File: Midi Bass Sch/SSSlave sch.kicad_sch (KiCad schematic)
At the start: 11 parts, among them J4 A SLAVE ISCP, J5 Pick Unit, U3 PIC16F1789

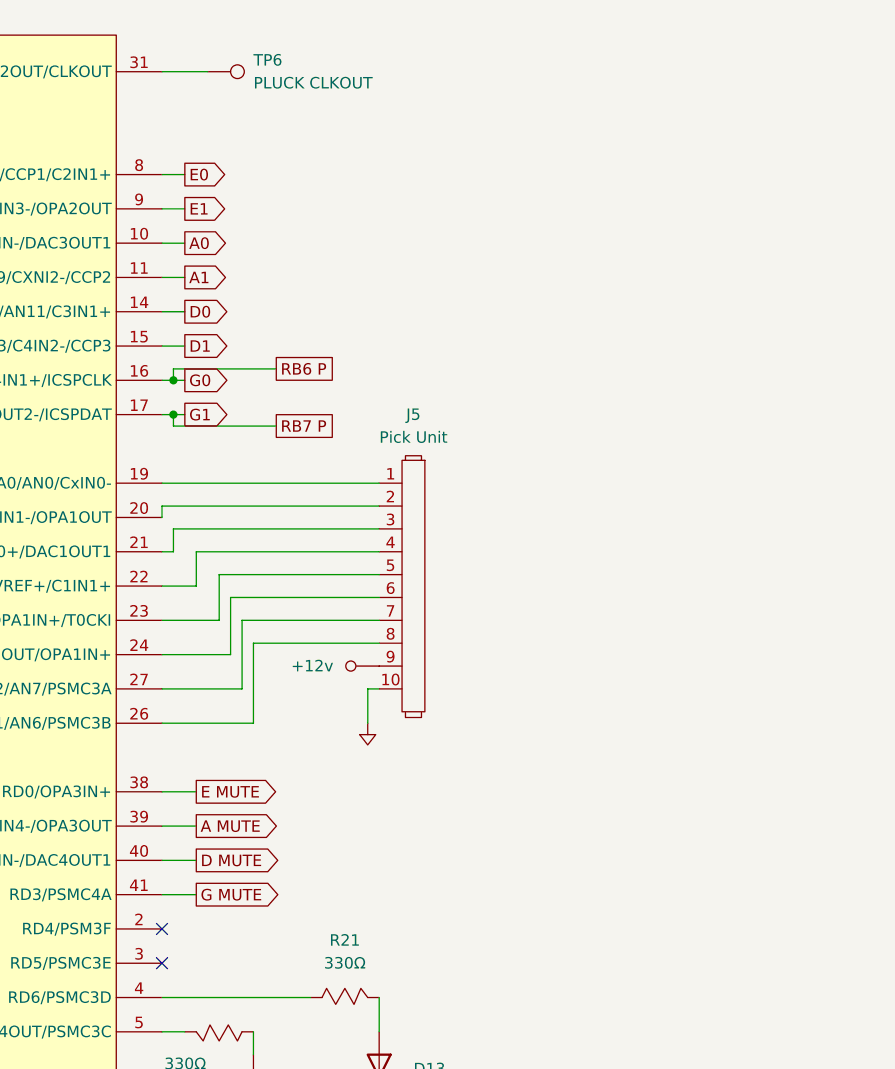
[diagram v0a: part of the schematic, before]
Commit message: working on final troubleshooting sections, modified pluck slave to header connections
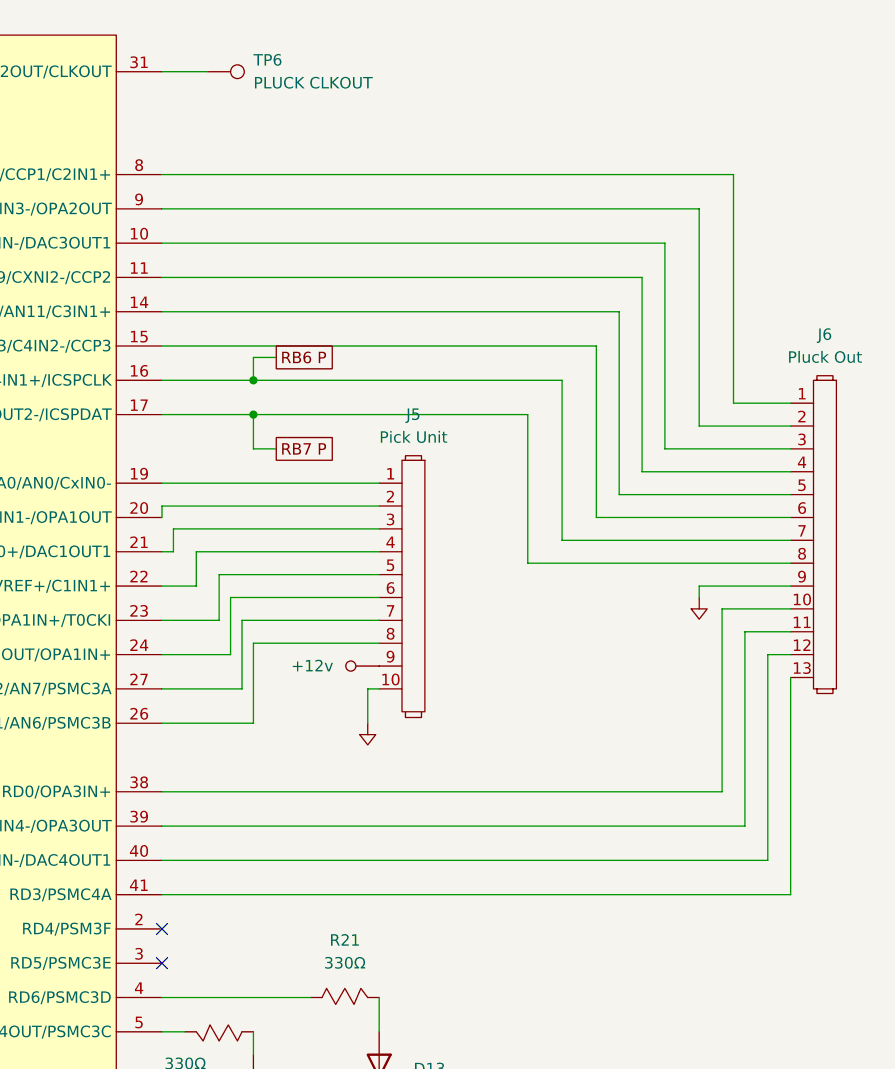
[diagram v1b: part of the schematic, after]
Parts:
- added J6: Pluck Out, symbol Owen's Symbols:Header_1x13
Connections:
- net GND: now also J6.9
- net A MUTE: no longer names the net of U3.39 (RD1/CxIN4-/OPA3OUT)
- net A MUTE: now also J6.11
- net A0: no longer names the net of U3.10 (RB2/AN8/OPA2IN-/DAC3OUT1)
- net A0: now also J6.3
- net A1: no longer names the net of U3.11 (RB3/AN9/CXNI2-/CCP2)
- net A1: now also J6.4
- net D MUTE: no longer names the net of U3.40 (RD2/OPA3IN-/DAC4OUT1)
- net D MUTE: now also J6.12
- net D0: no longer names the net of U3.14 (RB4/AN11/C3IN1+)
- net D0: now also J6.5
- net D1: no longer names the net of U3.15 (RB5/AN13/C4IN2-/CCP3)
- net D1: now also J6.6
- net E MUTE: no longer names the net of U3.38 (RD0/OPA3IN+)
- net E MUTE: now also J6.10
- net E0: no longer names the net of U3.8 (RB0/AN12/CCP1/C2IN1+)
- net E0: now also J6.1
- net E1: no longer names the net of U3.9 (RB1/AN10/CxIN3-/OPA2OUT)
- net E1: now also J6.2
- net G MUTE: no longer names the net of U3.41 (RD3/PSMC4A)
- net G MUTE: now also J6.13
- net G0 renamed RB6 P
- net RB6 P: now also J6.7
- net G1 renamed RB7 P
- net RB7 P: now also J6.8

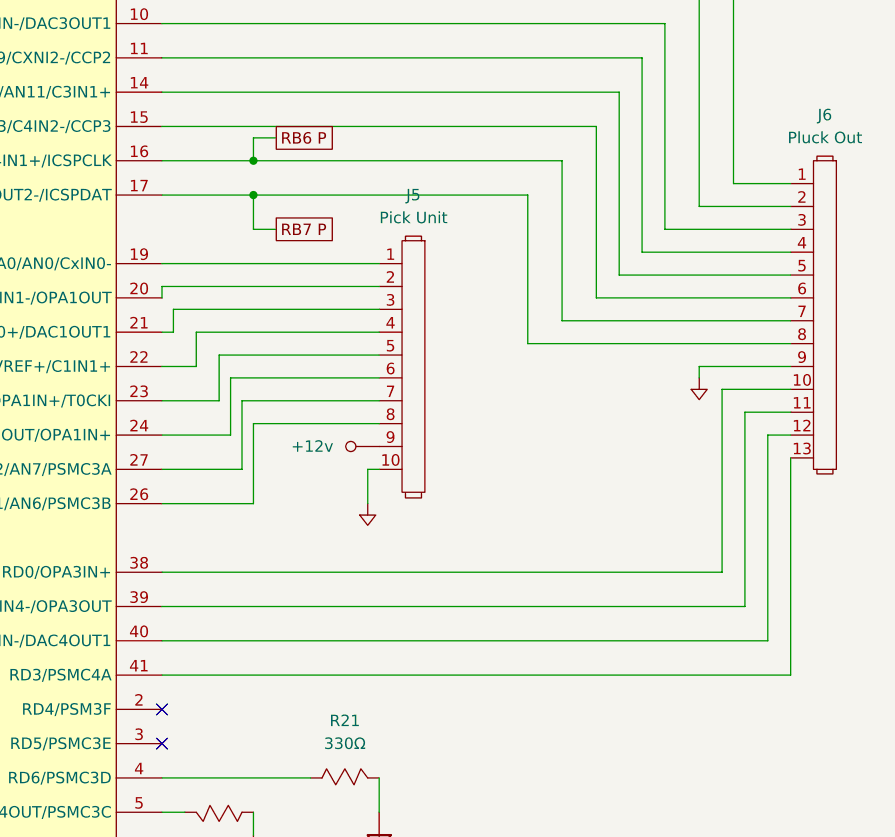
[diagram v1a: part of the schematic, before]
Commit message: updated plucking schematic to label line
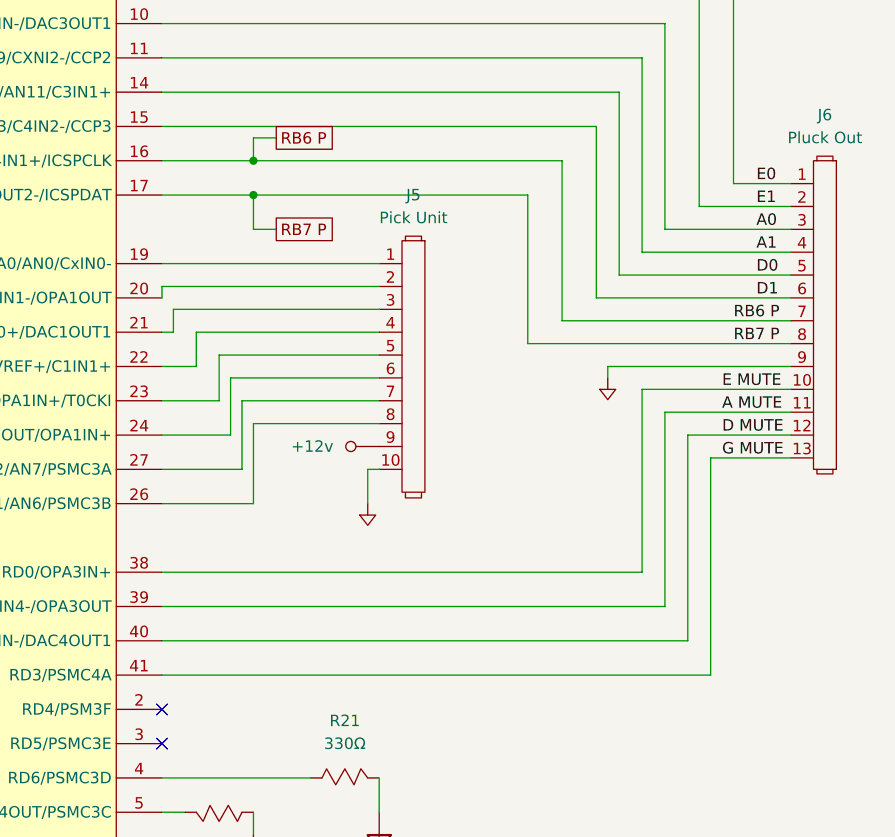
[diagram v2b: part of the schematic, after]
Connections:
- net A0: now reaches J6.3, U3.10 (RB2/AN8/OPA2IN-/DAC3OUT1)
- net A1: now reaches J6.4, U3.11 (RB3/AN9/CXNI2-/CCP2)
- net D0: now reaches J6.5, U3.14 (RB4/AN11/C3IN1+)
- net D1: now reaches J6.6, U3.15 (RB5/AN13/C4IN2-/CCP3)
- net E MUTE: now reaches J6.10, U3.38 (RD0/OPA3IN+)
- net A MUTE: now reaches J6.11, U3.39 (RD1/CxIN4-/OPA3OUT)
- net D MUTE: now reaches J6.12, U3.40 (RD2/OPA3IN-/DAC4OUT1)
- net G MUTE: now reaches J6.13, U3.41 (RD3/PSMC4A)
- net E0: now reaches J6.1, U3.8 (RB0/AN12/CCP1/C2IN1+)
- net E1: now reaches J6.2, U3.9 (RB1/AN10/CxIN3-/OPA2OUT)
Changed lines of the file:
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@@
 	(wire
 		(pts
-			(xy 228.6 92.71) (xy 233.68 92.71)
+			(xy 219.71 92.71) (xy 233.68 92.71)
 		)
 		(stroke
@@
 	(wire
 		(pts
-			(xy 233.68 121.92) (xy 233.68 97.79)
+			(xy 224.79 121.92) (xy 224.79 97.79)
 		)
 		(stroke
@@
 	(wire
 		(pts
-			(xy 228.6 114.3) (xy 228.6 92.71)
+			(xy 219.71 114.3) (xy 219.71 92.71)
 		)
 		(stroke
@@
 	(wire
 		(pts
-			(xy 163.83 118.11) (xy 231.14 118.11)
+			(xy 163.83 118.11) (xy 222.25 118.11)
 		)
 		(stroke
@@
 	(wire
 		(pts
-			(xy 226.06 110.49) (xy 226.06 90.17)
+			(xy 217.17 110.49) (xy 217.17 90.17)
 		)
 		(stroke
@@
 	(wire
 		(pts
-			(xy 163.83 121.92) (xy 233.68 121.92)
+			(xy 163.83 121.92) (xy 224.79 121.92)
 		)
 		(stroke
@@
 	(wire
 		(pts
-			(xy 233.68 87.63) (xy 223.52 87.63)
+			(xy 233.68 87.63) (xy 213.36 87.63)
 		)
 		(stroke
@@
 	(wire
 		(pts
-			(xy 231.14 118.11) (xy 231.14 95.25)
+			(xy 222.25 118.11) (xy 222.25 95.25)
 		)
 		(stroke
@@
 	(wire
 		(pts
-			(xy 231.14 95.25) (xy 233.68 95.25)
+			(xy 222.25 95.25) (xy 233.68 95.25)
 		)
 		(stroke
@@
 	(wire
 		(pts
-			(xy 163.83 110.49) (xy 226.06 110.49)
+			(xy 163.83 110.49) (xy 217.17 110.49)
 		)
 		(stroke
@@
 	(wire
 		(pts
-			(xy 226.06 90.17) (xy 233.68 90.17)
+			(xy 217.17 90.17) (xy 233.68 90.17)
 		)
 		(stroke
@@
 	(wire
 		(pts
-			(xy 163.83 114.3) (xy 228.6 114.3)
+			(xy 163.83 114.3) (xy 219.71 114.3)
 		)
 		(stroke
@@
 	(wire
 		(pts
-			(xy 223.52 87.63) (xy 223.52 88.9)
+			(xy 213.36 87.63) (xy 213.36 88.9)
 		)
 		(stroke
@@
 	(wire
 		(pts
+			(xy 224.79 97.79) (xy 233.68 97.79)
+		)
+		(stroke
+			(width 0)
+			(type default)
+		)
+	)
+	(wire
+		(pts
 			(xy 173.99 72.39) (xy 173.99 68.58)
 		)
@@
 			(width 0)
 			(type default)
+		)
+	)
+	(label "E0"
+		(at 229.87 67.31 0)
+		(fields_autoplaced yes)
+		(effects
+			(font
+				(size 1.27 1.27)
+			)
+			(justify left bottom)
+		)
+	)
+	(label "A1"
+		(at 229.87 74.93 0)
+		(fields_autoplaced yes)
+		(effects
+			(font
+				(size 1.27 1.27)
+			)
+			(justify left bottom)
+		)
+	)
+	(label "RB6 P"
+		(at 227.33 82.55 0)
+		(fields_autoplaced yes)
+		(effects
+			(font
+				(size 1.27 1.27)
+			)
+			(justify left bottom)
+		)
+	)
+	(label "E MUTE"
+		(at 226.06 90.17 0)
+		(fields_autoplaced yes)
+		(effects
+			(font
+				(size 1.27 1.27)
+			)
+			(justify left bottom)
+		)
+	)
+	(label "A0"
+		(at 229.87 72.39 0)
+		(fields_autoplaced yes)
+		(effects
+			(font
+				(size 1.27 1.27)
+			)
+			(justify left bottom)
+		)
+	)
+	(label "D0"
+		(at 229.87 77.47 0)
+		(fields_autoplaced yes)
+		(effects
+			(font
+				(size 1.27 1.27)
+			)
+			(justify left bottom)
+		)
+	)
+	(label "D MUTE"
+		(at 226.06 95.25 0)
+		(fields_autoplaced yes)
+		(effects
+			(font
+				(size 1.27 1.27)
+			)
+			(justify left bottom)
+		)
+	)
+	(label "E1"
+		(at 229.87 69.85 0)
+		(fields_autoplaced yes)
+		(effects
+			(font
+				(size 1.27 1.27)
+			)
+			(justify left bottom)
+		)
+	)
+	(label "A MUTE"
+		(at 226.06 92.71 0)
+		(fields_autoplaced yes)
+		(effects
+			(font
+				(size 1.27 1.27)
+			)
+			(justify left bottom)
+		)
+	)
+	(label "G MUTE"
+		(at 226.06 97.79 0)
+		(fields_autoplaced yes)
+		(effects
+			(font
+				(size 1.27 1.27)
+			)
+			(justify left bottom)
+		)
+	)
+	(label "RB7 P"
+		(at 227.33 85.09 0)
+		(fields_autoplaced yes)
+		(effects
+			(font
+				(size 1.27 1.27)
+			)
+			(justify left bottom)
+		)
+	)
+	(label "D1"
+		(at 229.87 80.01 0)
+		(fields_autoplaced yes)
+		(effects
+			(font
+				(size 1.27 1.27)
+			)
+			(justify left bottom)
 		)
 	)
@@
 	(symbol
 		(lib_id "Custom Power:GND")
-		(at 223.52 88.9 0)
+		(at 213.36 88.9 0)
 		(unit 1)
 		(exclude_from_sim no)
@@
 		(fields_autoplaced yes)
 		(property "Reference" "#PWR041"
-			(at 223.52 87.63 0)
+			(at 213.36 87.63 0)
 			(effects
 				(font
@@
 		)
 		(property "Value" "GND"
-			(at 223.52 87.63 0)
+			(at 213.36 87.63 0)
 			(effects
 				(font
@@
 		)
 		(property "Footprint" ""
-			(at 223.52 87.63 0)
+			(at 213.36 87.63 0)
 			(effects
 				(font
@@
 		)
 		(property "Datasheet" ""
-			(at 223.52 87.63 0)
+			(at 213.36 87.63 0)
 			(effects
 				(font
@@
 		)
 		(property "Description" ""
-			(at 223.52 88.9 0)
-			(effects
-				(font
+			(at 213.36 88.9 0)
+			(effects
+				(font

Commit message: finished troubleshooting section
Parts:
- renumbered J4 to J6, J5 to J7, J6 to J8
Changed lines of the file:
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@@
 		(dnp no)
 		(fields_autoplaced yes)
-		(property "Reference" "#PWR034"
+		(property "Reference" "#PWR036"
 			(at 55.88 133.35 0)
 			(effects
@@
 			(project "Midi Bass Sch"
 				(path "/06818073-fb22-48ee-acc5-6dedd827034e/673444b1-2638-4f61-b545-e7cdf999c0e0"
-					(reference "#PWR034")
+					(reference "#PWR036")
 					(unit 1)
 				)
@@
 		(dnp no)
 		(fields_autoplaced yes)
-		(property "Reference" "#PWR038"
+		(property "Reference" "#PWR040"
 			(at 182.9816 91.7956 0)
 			(effects
@@
 			(project ""
 				(path "/06818073-fb22-48ee-acc5-6dedd827034e/673444b1-2638-4f61-b545-e7cdf999c0e0"
-					(reference "#PWR038")
+					(reference "#PWR040")
 					(unit 1)
 				)
@@
 		(dnp no)
 		(fields_autoplaced yes)
-		(property "Reference" "#PWR040"
+		(property "Reference" "#PWR042"
 			(at 187.96 143.51 0)
 			(effects
@@
 			(project "Midi Bass Sch"
 				(path "/06818073-fb22-48ee-acc5-6dedd827034e/673444b1-2638-4f61-b545-e7cdf999c0e0"
-					(reference "#PWR040")
+					(reference "#PWR042")
 					(unit 1)
 				)
@@
 		(dnp no)
 		(fields_autoplaced yes)
-		(property "Reference" "J4"
+		(property "Reference" "J6"
 			(at 34.29 58.42 0)
 			(effects
@@
 			(project "Midi Bass Sch"
 				(path "/06818073-fb22-48ee-acc5-6dedd827034e/673444b1-2638-4f61-b545-e7cdf999c0e0"
-					(reference "J4")
+					(reference "J6")
 					(unit 1)
 				)
@@
 		(dnp no)
 		(fields_autoplaced yes)
-		(property "Reference" "#PWR033"
+		(property "Reference" "#PWR035"
 			(at 60.6044 111.8616 0)
 			(effects
@@
 			(project "Midi Bass Sch"
 				(path "/06818073-fb22-48ee-acc5-6dedd827034e/673444b1-2638-4f61-b545-e7cdf999c0e0"
-					(reference "#PWR033")
+					(reference "#PWR035")
 					(unit 1)
 				)
@@
 		(dnp no)
 		(fields_autoplaced yes)
-		(property "Reference" "#PWR036"
+		(property "Reference" "#PWR038"
 			(at 115.57 149.86 0)
 			(effects
@@
 			(project "Midi Bass Sch"
 				(path "/06818073-fb22-48ee-acc5-6dedd827034e/673444b1-2638-4f61-b545-e7cdf999c0e0"
-					(reference "#PWR036")
+					(reference "#PWR038")
 					(unit 1)
 				)
@@
 		(dnp no)
 		(fields_autoplaced yes)
-		(property "Reference" "#PWR035"
+		(property "Reference" "#PWR037"
 			(at 117.7544 15.3416 0)
 			(effects
@@
 			(project "Midi Bass Sch"
 				(path "/06818073-fb22-48ee-acc5-6dedd827034e/673444b1-2638-4f61-b545-e7cdf999c0e0"
-					(reference "#PWR035")
+					(reference "#PWR037")
 					(unit 1)
 				)
@@
 		(on_board yes)
 		(dnp no)
-		(property "Reference" "J5"
+		(property "Reference" "J7"
 			(at 191.77 68.58 0)
 			(effects
@@
 			(project ""
 				(path "/06818073-fb22-48ee-acc5-6dedd827034e/673444b1-2638-4f61-b545-e7cdf999c0e0"
-					(reference "J5")
+					(reference "J7")
 					(unit 1)
 				)
@@
 		(dnp no)
 		(fields_autoplaced yes)
-		(property "Reference" "#PWR032"
+		(property "Reference" "#PWR034"
 			(at 45.72 71.12 0)
 			(effects
@@
 			(project "Midi Bass Sch"
 				(path "/06818073-fb22-48ee-acc5-6dedd827034e/673444b1-2638-4f61-b545-e7cdf999c0e0"
-					(reference "#PWR032")
+					(reference "#PWR034")
 					(unit 1)
 				)
@@
 		(dnp no)
 		(fields_autoplaced yes)
-		(property "Reference" "#PWR041"
+		(property "Reference" "#PWR043"
 			(at 213.36 87.63 0)
 			(effects
@@
 			(project "Midi Bass Sch"
 				(path "/06818073-fb22-48ee-acc5-6dedd827034e/673444b1-2638-4f61-b545-e7cdf999c0e0"
-					(reference "#PWR041")
+					(reference "#PWR043")
 					(unit 1)
 				)
@@
 		(dnp no)
 		(fields_autoplaced yes)
-		(property "Reference" "#PWR039"
+		(property "Reference" "#PWR041"
 			(at 186.69 101.6 0)
 			(effects
@@
 			(project "Midi Bass Sch"
 				(path "/06818073-fb22-48ee-acc5-6dedd827034e/673444b1-2638-4f61-b545-e7cdf999c0e0"
-					(reference "#PWR039")
+					(reference "#PWR041")
 					(unit 1)
 				)
@@
 		(dnp no)
 		(fields_autoplaced yes)
-		(property "Reference" "#PWR037"
+		(property "Reference" "#PWR039"
 			(at 173.99 146.05 0)
 			(effects
@@
 			(project "Midi Bass Sch"
 				(path "/06818073-fb22-48ee-acc5-6dedd827034e/673444b1-2638-4f61-b545-e7cdf999c0e0"
-					(reference "#PWR037")
+					(reference "#PWR039")
 					(unit 1)
 				)
@@
 		(on_board yes)
 		(dnp no)
-		(property "Reference" "J6"
+		(property "Reference" "J8"
 			(at 237.49 59.69 0)
 			(effects
@@
 			(project ""
 				(path "/06818073-fb22-48ee-acc5-6dedd827034e/673444b1-2638-4f61-b545-e7cdf999c0e0"
-					(reference "J6")
+					(reference "J8")
 					(unit 1)
 				)
@@
 		(dnp no)
 		(fields_autoplaced yes)
-		(property "Reference" "#PWR031"
+		(property "Reference" "#PWR033"
 			(at 50.4444 58.5216 0)
 			(effects
@@
 			(project "Midi Bass Sch"
 				(path "/06818073-fb22-48ee-acc5-6dedd827034e/673444b1-2638-4f61-b545-e7cdf999c0e0"
-					(reference "#PWR031")
-					(unit 1)
-				)
+					(reference "#PWR033")
+					(unit 1)
+				)

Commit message: finished BOM
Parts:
- J6: value A SLAVE ISCP -> Pluck ISCP
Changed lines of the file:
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@@
 			)
 		)
-		(property "Value" "A SLAVE ISCP"
+		(property "Value" "Pluck ISCP"
 			(at 34.29 60.96 0)
 			(effects

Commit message: began getting images for schematic appendix
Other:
- title: (none) -> Plucking Processor Schematic
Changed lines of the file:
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@@
 	(generator_version "8.0")
 	(paper "A")
+	(title_block
+		(title "Plucking Processor Schematic")
+		(date "2024-12-10")
+		(rev "A")
+	)
 	(junction
 		(at 55.88 127)

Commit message: began working on pcb layout deleted extra schematics for solenoid break out board
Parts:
- J7: footprint (none) -> Connector_PinHeader_2.54mm:PinHeader_1x10_P2.54mm_Vertical
- J8: footprint (none) -> Connector_PinHeader_2.54mm:PinHeader_1x13_P2.54mm_Vertical
- TP6: footprint (none) -> Connector_PinHeader_2.54mm:PinHeader_1x01_P2.54mm_Vertical
- U3: footprint (none) -> OF footprints:TQFN-44_7x7_Pitch0.4mm
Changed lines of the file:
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@@
 			)
 		)
-		(property "Footprint" ""
+		(property "Footprint" "Connector_PinHeader_2.54mm:PinHeader_1x01_P2.54mm_Vertical"
 			(at 168.91 35.56 0)
 			(effects
@@
 			)
 		)
-		(property "Footprint" ""
+		(property "Footprint" "Connector_PinHeader_2.54mm:PinHeader_1x10_P2.54mm_Vertical"
 			(at 191.77 72.39 0)
 			(effects
@@
 			)
 		)
-		(property "Footprint" ""
+		(property "Footprint" "OF footprints:TQFN-44_7x7_Pitch0.4mm"
 			(at 87.63 36.83 0)
 			(effects
@@
 			)
 		)
-		(property "Footprint" ""
+		(property "Footprint" "Connector_PinHeader_2.54mm:PinHeader_1x13_P2.54mm_Vertical"
 			(at 237.49 63.5 0)
 			(effects

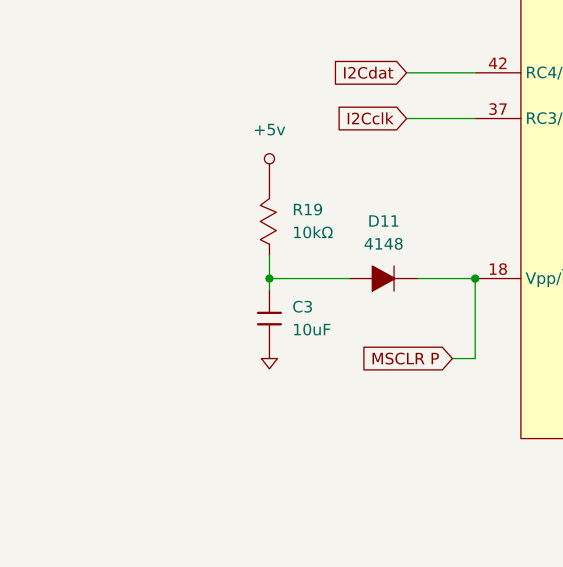
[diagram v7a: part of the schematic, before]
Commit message: created pcb for breakout working on pcb for main control board
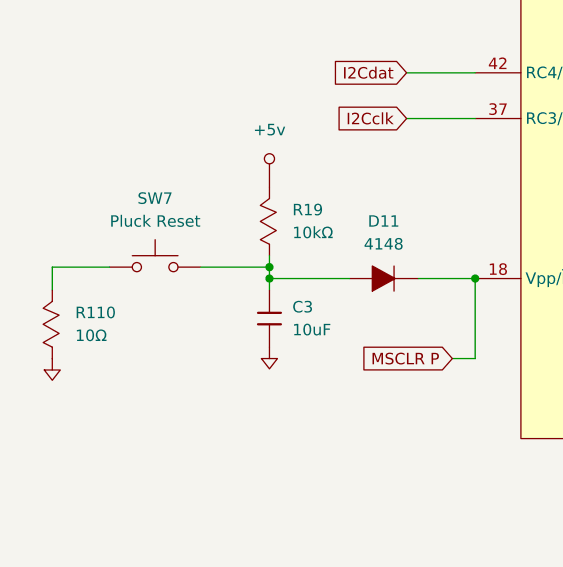
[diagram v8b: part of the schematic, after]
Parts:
- added R110: 10Ω, Resistor_SMD:R_0805_2012Metric_Pad1.20x1.40mm_HandSolder, symbol Owen's Symbols:Resistor_Mod
- added SW7: Pluck Reset, Button_Switch_THT:SW_PUSH_6mm_H5mm, symbol Switch:SW_Push
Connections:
- net GND: now also R110.1
- net at C3.1, D11.2, R19.1: now also SW7.2
- new net: R110.2, SW7.1
